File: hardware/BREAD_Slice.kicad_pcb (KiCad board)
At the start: 2 copper layers, 72.6 x 100 mm, 16 parts, among them J1 Conn_01x10_Female, J2 I2C_01x04

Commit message: Initial commit
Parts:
- removed C3, C4: 22uF, Capacitor_SMD:C_1206_3216Metric
- removed D1: WS2812B_5050, SparkFun-LED:WS2812-5050-4PIN
- removed HS1: Heatsink_Pad, SparkFun-Fuse:Thermal Pad
- removed L1: 4.7uH, Inductor_SMD:L_1210_3225Metric
- removed U1: ~, Package_TO_SOT_SMD:TSOT-23-6
- added J3: Screw_Terminal_01x03, TerminalBlock_TE-Connectivity:TerminalBlock_TE_282834-3_1x03_P2.54mm_Horizontal, F.Cu at (184.3, 88.1)
- added J4: Screw_Terminal_01x03, TerminalBlock_TE-Connectivity:TerminalBlock_TE_282834-3_1x03_P2.54mm_Horizontal, F.Cu at (184.3, 64.0)
- added J5: Screw_Terminal_01x03, TerminalBlock_TE-Connectivity:TerminalBlock_TE_282834-3_1x03_P2.54mm_Horizontal, F.Cu at (184.3, 100.2)
- added J6: Screw_Terminal_01x03, TerminalBlock_TE-Connectivity:TerminalBlock_TE_282834-3_1x03_P2.54mm_Horizontal, F.Cu at (184.3, 76.0)
- added J7: Conn_01x03_Male, Connector_PinSocket_2.54mm:PinSocket_1x03_P2.54mm_Vertical, F.Cu at (184.3, 112.5)
- added J8: Screw_Terminal_01x02, TerminalBlock_TE-Connectivity:TerminalBlock_TE_282834-2_1x02_P2.54mm_Horizontal, F.Cu at (184.3, 122.3)
- C1: value 22uF -> 10uF_t; footprint Capacitor_SMD:C_1206_3216Metric -> OCI_UPL_FOOTPRINTS:C_2312
- C2: value 100nF -> 10uF_t; footprint Capacitor_SMD:C_1206_3216Metric -> OCI_UPL_FOOTPRINTS:C_2312
- H1, H4: footprint MountingHole:MountingHole_5mm -> MountingHole:MountingHole_3.2mm_M3_DIN965_Pad
- H2: renamed from H3; footprint MountingHole:MountingHole_5mm -> MountingHole:MountingHole_3.2mm_M3_DIN965_Pad
- H3: renamed from H2; footprint MountingHole:MountingHole_5mm -> MountingHole:MountingHole_3.2mm_M3_DIN965_Pad
- J2: value I2C_01x04 -> Screw_Terminal_01x03; footprint Connector_JST:JST_SH_SM04B-SRSS-TB_1x04-1MP_P1.00mm_Horizontal -> TerminalBlock_TE-Connectivity:TerminalBlock_TE_282834-3_1x03_P2.54mm_Horizontal; moved to F.Cu
- moved J2 91.1 mm to (184.3, 51.9), turned to -90 degrees
- moved Logo1 75.1 mm to (166.6, 135.8), turned to 0 degrees
- moved C1 33.9 mm to (154.2, 97.4), turned to 90 degrees
- moved C2 28.1 mm to (154.2, 110.2), turned to -90 degrees
- moved A1 7.59 mm to (135.0, 100.0)
- moved J1 3.43 mm to (129.6, 78.8)
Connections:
- A1 pad 1: unconnected-(A1-D1/TX-Pad1) -> Net-(A1-Pad1)
- A1 pad 10: unconnected-(A1-D7-Pad10) -> Net-(A1-Pad10)
- A1 pad 11: unconnected-(A1-D8-Pad11) -> Net-(A1-Pad11)
- A1 pad 12: unconnected-(A1-D9-Pad12) -> /PWM3
- A1 pad 13: unconnected-(A1-D10-Pad13) -> /PWM4
- A1 pad 14: unconnected-(A1-D11-Pad14) -> /PWM5
- A1 pad 15: unconnected-(A1-D12-Pad15) -> Net-(A1-Pad15)
- A1 pad 16: unconnected-(A1-D13-Pad16) -> Net-(A1-Pad16)
- A1 pad 17: unconnected-(A1-3V3-Pad17) -> Net-(A1-Pad17)
- A1 pad 18: unconnected-(A1-AREF-Pad18) -> Net-(A1-Pad18)
- A1 pad 19: unconnected-(A1-A0-Pad19) -> Net-(A1-Pad19)
- A1 pad 2: unconnected-(A1-D0/RX-Pad2) -> Net-(A1-Pad2)
- A1 pad 20: unconnected-(A1-A1-Pad20) -> Net-(A1-Pad20)
- A1 pad 21: unconnected-(A1-A2-Pad21) -> Net-(A1-Pad21)
- A1 pad 22: unconnected-(A1-A3-Pad22) -> Net-(A1-Pad22)
- A1 pad 25: unconnected-(A1-A6-Pad25) -> Net-(A1-Pad25)
- A1 pad 26: unconnected-(A1-A7-Pad26) -> Net-(A1-Pad26)
- A1 pad 28: unconnected-(A1-~{RESET}-Pad28) -> Net-(A1-Pad28)
- A1 pad 3: unconnected-(A1-~{RESET}-Pad3) -> Net-(A1-Pad3)
- A1 pad 30: unconnected-(A1-VIN-Pad30) -> +12V
- A1 pad 8: /LED -> /PWM1
- A1 pad 9: unconnected-(A1-D6-Pad9) -> /PWM2
- C1 pad 1: GND -> +12V
- C1 pad 2: +12V -> GND
- C2 pad 1: Net-(U1-SW) -> +5V
- C2 pad 2: Net-(U1-BST) -> GND
- J2 pad 1: GND -> /PWM1
- J2 pad 2: +5V -> /PWR
- J2 pad 3: /I2C_DAT -> GND
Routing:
- net /PWM1: track 0.00 -> 119.3 mm, vias 0 -> 2
- net GND: track 19.6 -> 138.1 mm, vias 14 -> 0
- net /PWM2: track 0.00 -> 110.1 mm, vias 0 -> 2
- net /PWM3: track 0.00 -> 105.4 mm, vias 0 -> 2
- net +5V: track 108.9 -> 3.99 mm, vias 1 -> 0
- net /PWM4: track 0.00 -> 99.2 mm, vias 0 -> 2
- net /PWM5: track 0.00 -> 97.8 mm, vias 0 -> 2
- net /LED: track 51.5 -> 0.00 mm
- net +12V: track 46.8 -> 97.2 mm
- net /I2C_CLK: track 78.5 -> 43.0 mm, vias 2 -> 0
- net /I2C_DAT: track 76.6 -> 43.1 mm, vias 2 -> 0
- net /CSTM: track 0.00 -> 11.8 mm
- net /E_STOP: track 30.1 -> 21.6 mm
- net /INT: track 28.8 -> 21.7 mm
- net /SYNC: track 27.9 -> 21.5 mm
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- added copper zone on B.Cu, net /PWR
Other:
- board size 72.6 x 100 mm -> 70 x 100 mm
- board text added: "- +"
- board text added: "12V CSTM IN"
- board text added: "CSTM IN"
- board text added: "GND PWR PWM"
- board text added: "M1"
- board text added: "M2"
- board text added: "M3"
- board text added: "M4"
- board text added: "M5"
- board text added: "PWR SEL"
- board text added: "Servo Slice SLC_SERV R0 2021"
- board text removed: "12V"
- board text removed: "12V->5V Reg"
- board text removed: "5V I2C Connector"
- board text removed: "ARDUINO NANO"
- board text removed: "BREAD Slice Template SLC_TEMP <version> <year>"
- board text removed: "ESTOP"
- board text removed: "GND"
- board text removed: "INT"
- board text removed: "LED"
- board text removed: "SCL"
- board text removed: "SDA"
- board text removed: "SYNC"

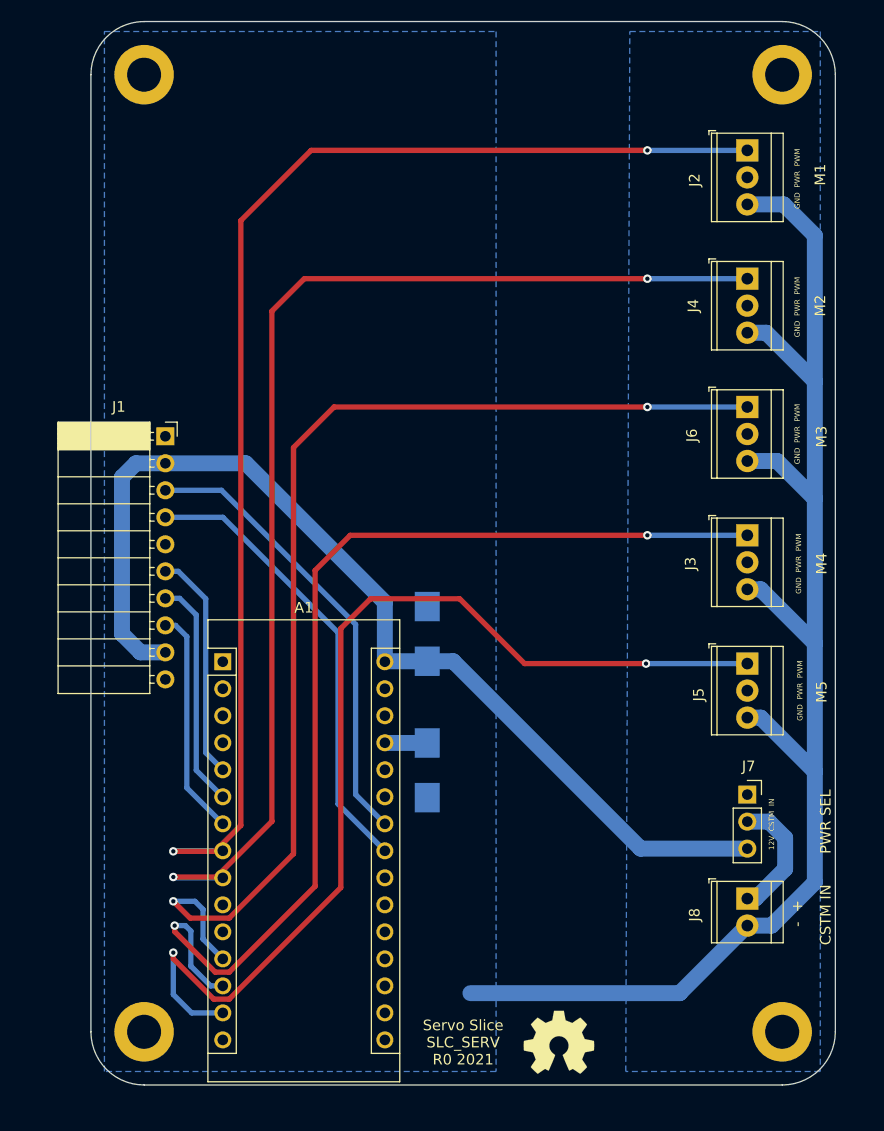
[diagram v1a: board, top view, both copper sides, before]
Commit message: changed custom selection method to be correct and offer 5V, new BREAD core
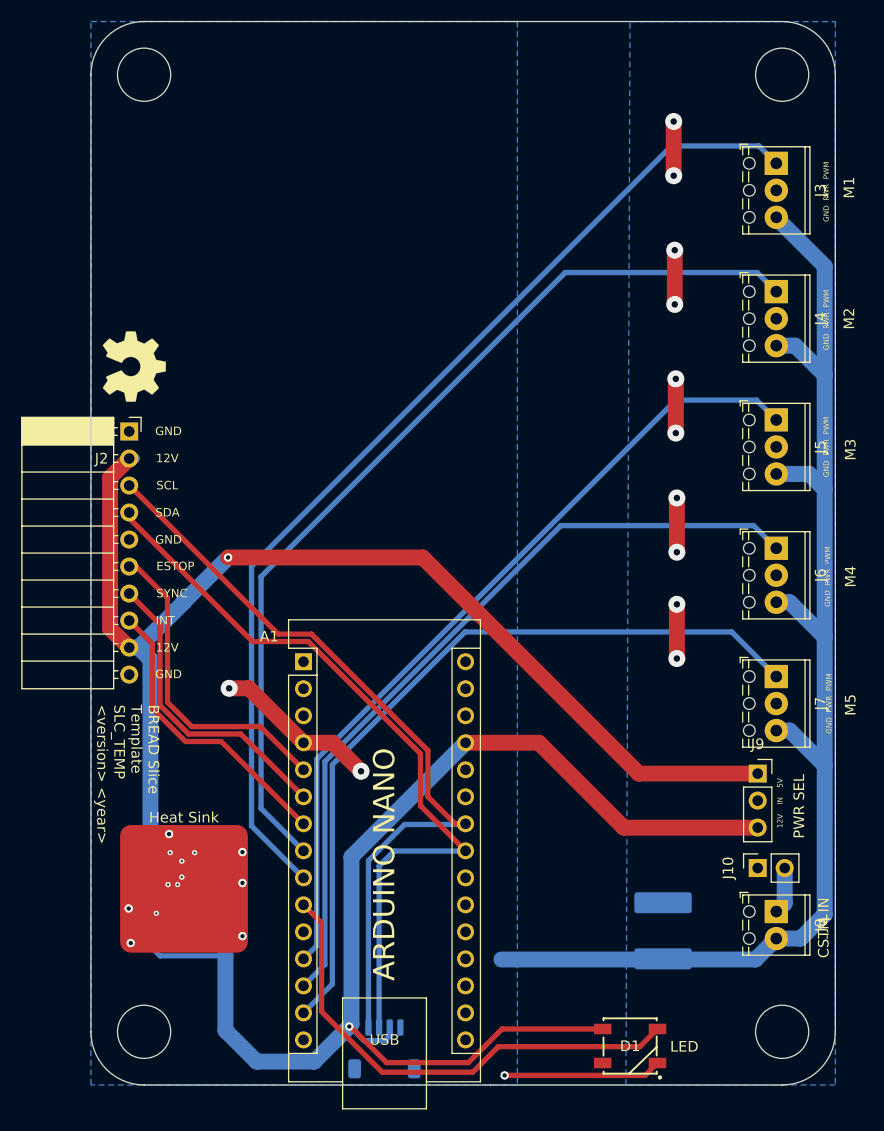
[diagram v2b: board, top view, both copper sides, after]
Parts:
- removed the J2 at (184.3, 51.9)
- added C3: 22uF, Capacitor_SMD:C_1206_3216Metric, B.Cu at (133.8, 119.5)
- added C4: 22uF, Capacitor_SMD:C_1206_3216Metric, B.Cu at (133.8, 116.5)
- added C5: 10uF_t, Capacitor_SMD:C_2220_5750Metric_Pad1.97x5.40mm_HandSolder, B.Cu at (176.4, 125.3)
- added D1: WS2812B_5050, SparkFun-LED:WS2812-5050-4PIN, F.Cu at (173.3, 136.1)
- added HS1: Heatsink_Pad, KML-Custom:Thermal Pad, F.Cu at (131.3, 121.4)
- added J1: I2C_01x04, Connector_JST:JST_SH_SM04B-SRSS-TB_1x04-1MP_P1.00mm_Horizontal, B.Cu at (150.2, 136.4)
- added J10: Conn_01x02_Pin, Connector_PinSocket_2.54mm:PinSocket_1x02_P2.54mm_Vertical, F.Cu at (185.3, 119.4)
- added J9: Conn_01x03_Male, Connector_PinSocket_2.54mm:PinSocket_1x03_P2.54mm_Vertical, F.Cu at (185.3, 110.5)
- added L1: 4.7uH, Inductor_SMD:L_1210_3225Metric, B.Cu at (133.8, 122.8)
- added U1: ~, Package_TO_SOT_SMD:TSOT-23-6, B.Cu at (128.8, 122.8)
- C1: value 10uF_t -> 22uF; footprint OCI_UPL_FOOTPRINTS:C_2312 -> Capacitor_SMD:C_1206_3216Metric
- C2: value 10uF_t -> 100nF; footprint OCI_UPL_FOOTPRINTS:C_2312 -> Capacitor_SMD:C_1206_3216Metric
- H1, H4: footprint MountingHole:MountingHole_3.2mm_M3_DIN965_Pad -> MountingHole:MountingHole_5mm
- H2: renamed from H3; footprint MountingHole:MountingHole_3.2mm_M3_DIN965_Pad -> MountingHole:MountingHole_5mm
- H3: renamed from H2; footprint MountingHole:MountingHole_3.2mm_M3_DIN965_Pad -> MountingHole:MountingHole_5mm
- J3, J4, J5, J6: footprint TerminalBlock_TE-Connectivity:TerminalBlock_TE_282834-3_1x03_P2.54mm_Horizontal -> TerminalBlock_Phoenix:TerminalBlock_Phoenix_MPT-0,5-3-2.54_1x03_P2.54mm_Horizontal
- J7: value Conn_01x03_Male -> Screw_Terminal_01x03; footprint Connector_PinSocket_2.54mm:PinSocket_1x03_P2.54mm_Vertical -> TerminalBlock_Phoenix:TerminalBlock_Phoenix_MPT-0,5-3-2.54_1x03_P2.54mm_Horizontal
- J8: footprint TerminalBlock_TE-Connectivity:TerminalBlock_TE_282834-2_1x02_P2.54mm_Horizontal -> TerminalBlock_Phoenix:TerminalBlock_Phoenix_MPT-0,5-2-2.54_1x02_P2.54mm_Horizontal
- moved Logo1 75.1 mm to (126.7, 72.2), turned to -90 degrees
- moved J3 35.1 mm to (187.1, 53.1)
- moved C1 33.9 mm to (128.6, 119.5), turned to 180 degrees
- moved C2 28.1 mm to (131.2, 126.3), turned to 180 degrees
- moved J5 23.1 mm to (187.1, 77.3)
- moved J6 13.6 mm to (187.1, 89.3)
- moved J7 11.4 mm to (187.1, 101.4), turned to -90 degrees
- moved A1 7.59 mm to (142.6, 100.0)
- moved J2 3.43 mm to (126.2, 78.3)
- moved J8 2.99 mm to (187.1, 123.5)
- moved J4 2.99 mm to (187.1, 65.2)
- renumbered J1 to J2
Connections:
- A1 pad 1: Net-(A1-Pad1) -> unconnected-(A1-D1/TX-Pad1)
- A1 pad 10: Net-(A1-Pad10) -> /LED
- A1 pad 11: Net-(A1-Pad11) -> unconnected-(A1-D8-Pad11)
- A1 pad 15: Net-(A1-Pad15) -> unconnected-(A1-D12-Pad15)
- A1 pad 16: Net-(A1-Pad16) -> unconnected-(A1-D13-Pad16)
- A1 pad 17: Net-(A1-Pad17) -> unconnected-(A1-3V3-Pad17)
- A1 pad 18: Net-(A1-Pad18) -> unconnected-(A1-AREF-Pad18)
- A1 pad 19: Net-(A1-Pad19) -> unconnected-(A1-A0-Pad19)
- A1 pad 2: Net-(A1-Pad2) -> unconnected-(A1-D0/RX-Pad2)
- A1 pad 20: Net-(A1-Pad20) -> unconnected-(A1-A1-Pad20)
- A1 pad 21: Net-(A1-Pad21) -> unconnected-(A1-A2-Pad21)
- A1 pad 22: Net-(A1-Pad22) -> unconnected-(A1-A3-Pad22)
- A1 pad 25: Net-(A1-Pad25) -> unconnected-(A1-A6-Pad25)
- A1 pad 26: Net-(A1-Pad26) -> unconnected-(A1-A7-Pad26)
- A1 pad 28: Net-(A1-Pad28) -> unconnected-(A1-~{RESET}-Pad28)
- A1 pad 3: Net-(A1-Pad3) -> unconnected-(A1-~{RESET}-Pad3)
- A1 pad 30: +12V -> unconnected-(A1-VIN-Pad30)
- A1 pad 8: /PWM1 -> /PWM2
- A1 pad 9: /PWM2 -> /PWM1
- C1 pad 1: +12V -> GND
- C1 pad 2: GND -> +12V
- C2 pad 1: +5V -> Net-(U1-SW)
- C2 pad 2: GND -> Net-(U1-BST)
- J3 pad 1: /PWM4 -> /PWM1
- J5 pad 1: /PWM5 -> /PWM3
- J6 pad 1: /PWM3 -> /PWM4
- J6 pad 2: Net-(J6-Pad2) -> /PWR
- J7 pad 1: /PWR -> /PWM5
- J7 pad 2: /CSTM -> /PWR
- J7 pad 3: +12V -> GND
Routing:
- net +5V: track 3.99 -> 137.4 mm, vias 0 -> 1
- net /LED: track 0.00 -> 46.4 mm
- net GND: track 138.1 -> 169.3 mm, vias 0 -> 16
- net /I2C_CLK: track 43.0 -> 73.6 mm
- net /I2C_DAT: track 43.1 -> 71.9 mm
- net /PWM3: track 105.4 -> 77.3 mm, vias 2 -> 0
- net /PWR: track 0.00 -> 25.5 mm, vias 0 -> 10
- net /PWM4: track 99.2 -> 74.4 mm, vias 2 -> 0
- net /PWM5: track 97.8 -> 73.1 mm, vias 2 -> 0
- net /PWM1: track 119.3 -> 97.7 mm, vias 2 -> 0
- net /PWM2: track 110.1 -> 88.6 mm, vias 2 -> 0
- net +12V: track 97.2 -> 116.0 mm, vias 0 -> 1
- net /E_STOP: track 21.6 -> 30.1 mm
- net /CSTM: track 11.8 -> 4.42 mm
- net /INT: track 21.7 -> 28.8 mm
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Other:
- outline, holes or cut-outs redrawn
- board text added: "12V"
- board text added: "12V IN 5V"
- board text added: "12V->5V Reg"
- board text added: "5V I2C Connector"
- board text added: "ARDUINO NANO"
- board text added: "BREAD Slice Template SLC_TEMP <version> <year>"
- board text added: "ESTOP"
- board text added: "GND"
- board text added: "INT"
- board text added: "LED"
- board text added: "SCL"
- board text added: "SDA"
- board text added: "SYNC"
- board text removed: "12V CSTM IN"
- board text removed: "Servo Slice SLC_SERV R0 2021"

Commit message: JLCPCB order rev-A
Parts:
- added G***: LOGO, LOGO, F.Cu at (152.8, 68.1)
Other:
- board text added: "BREAD Slice Servo Control (SLC_SERV) Cam K Brooks rev.A [09-2024]"
- board text removed: "BREAD Slice Template SLC_TEMP <version> <year>"
